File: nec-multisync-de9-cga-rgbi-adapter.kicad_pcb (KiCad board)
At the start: 2 copper layers, 52.1 x 36.1 mm, 8 parts, among them J1 DE9_Plug, J2 DE15_Receptacle_HighDensity, J3 DIN-8

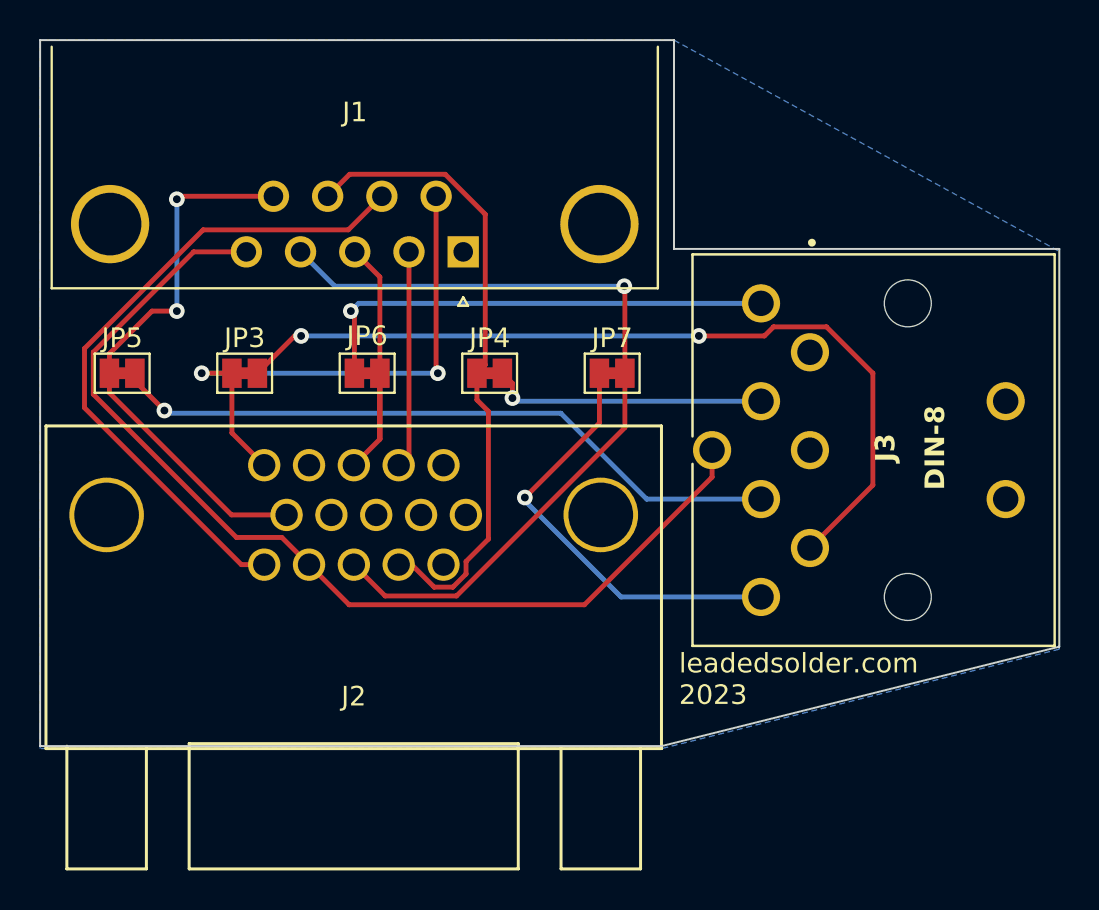
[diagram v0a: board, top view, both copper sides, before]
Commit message: Tie shields together
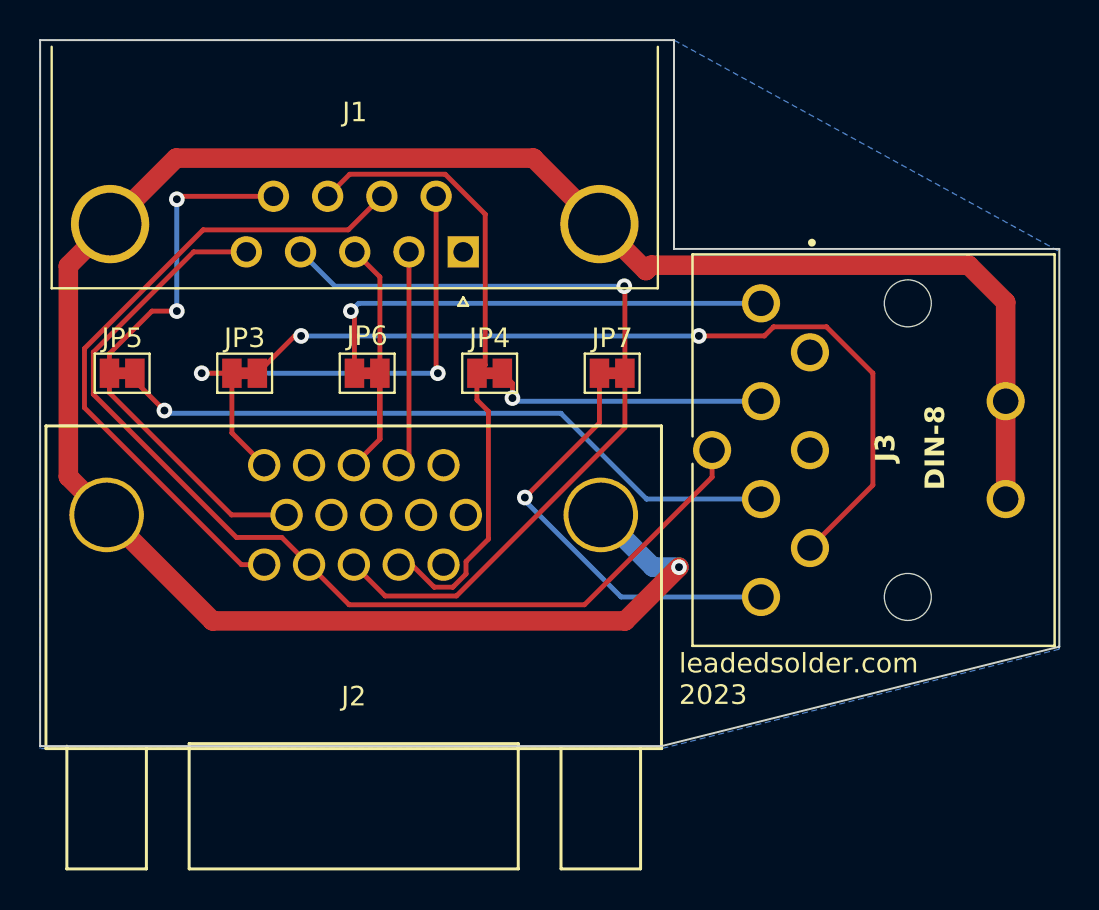
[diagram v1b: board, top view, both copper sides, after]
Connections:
- J1 pad 0: GND -> /Shield
- J2 pad 16: GND -> /Shield
- J2 pad 17: GND -> /Shield
- J3 pad S1: GND -> /Shield
- J3 pad S2: GND -> /Shield
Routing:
- net /Shield: track 0.00 -> 114.8 mm, vias 0 -> 1
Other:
- board text added: "rgbi to nec multisync adapter v0.3"
- board text removed: "rgbi to nec multisync adapter v0.2"
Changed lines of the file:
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@@
   (net 20 "/P6_Red")
   (net 21 "/P6_Green")
+  (net 22 "/Shield")
   (footprint "Jumper:SolderJumper-2_P1.3mm_Bridged_Pad1.0x1.5mm" (layer "F.Cu")
     (at 119.126 90.17)
@@
       (net 7 "/EGA_Blue1") (pintype "passive"))
     (pad "16" thru_hole circle (at 12.6238 11.811 180) (size 3.81 3.81) (drill 3.302) (layers "*.Cu" "*.Mask")
-      (net 1 "GND"))
+      (net 22 "/Shield") (pinfunction "Shield") (pintype "power_in"))
     (pad "17" thru_hole circle (at -12.6238 11.811 180) (size 3.81 3.81) (drill 3.302) (layers "*.Cu" "*.Mask")
-      (net 1 "GND"))
+      (net 22 "/Shield") (pinfunction "Shield") (pintype "power_in"))
     (model "${KICAD7_3DMODEL_DIR}/Connector_Dsub.3dshapes/DSUB-15-HD_Female_Horizontal_P2.29x1.98mm_EdgePinOffset9.40mm.step"
       (offset (xyz -4.5 -13.5 0))
@@
       (net 5 "/EGA_Blue0") (pintype "passive"))
     (pad "S1" thru_hole circle (at -2.5 10 90) (size 1.95 1.95) (drill 1.3) (layers "*.Cu" "*.Mask")
-      (net 1 "GND"))
+      (net 22 "/Shield") (pinfunction "Shield") (pintype "power_in"))
     (pad "S2" thru_hole circle (at 2.5 10 90) (size 1.95 1.95) (drill 1.3) (layers "*.Cu" "*.Mask")
-      (net 1 "GND"))
+      (net 22 "/Shield") (pinfunction "Shield") (pintype "power_in"))
   )
   (footprint "Connector_Dsub:DSUB-9_Male_Horizontal_P2.77x2.84mm_EdgePinOffset7.70mm_Housed_MountingHolesOffset9.12mm" (layer "F.Cu")
@@
       (stroke (width 0.1) (type solid)) (layer "F.Fab"))
     (pad "0" thru_hole circle (at -6.96 1.42 180) (size 4 4) (drill 3.2) (layers "*.Cu" "*.Mask")
-      (net 1 "GND"))
+      (net 22 "/Shield") (pinfunction "Shield") (pintype "power_in"))
     (pad "0" thru_hole circle (at 18.04 1.42 180) (size 4 4) (drill 3.2) (layers "*.Cu" "*.Mask")
-      (net 1 "GND"))
+      (net 22 "/Shield") (pinfunction "Shield") (pintype "power_in"))
     (pad "1" thru_hole rect (at 0 0 180) (size 1.6 1.6) (drill 1) (layers "*.Cu" "*.Mask")
       (net 1 "GND") (pinfunction "1") (pintype "passive"))
@@
     (effects (font (size 1 1) (thickness 0.15)) (justify left bottom mirror))
   )
-  (gr_text "rgbi to nec multisync adapter v0.2" (at 131.000001 89.408 180) (layer "B.SilkS" knockout)
+  (gr_text "rgbi to nec multisync adapter v0.3" (at 131.000001 89.408 180) (layer "B.SilkS" knockout)
     (effects (font (size 1 1) (thickness 0.15)) (justify mirror))
   )
@@
   (segment (start 139.7 96.683097) (end 139.7 96.52) (width 0.25) (layer "B.Cu") (net 21))
   (segment (start 144.616903 101.6) (end 139.7 96.683097) (width 0.25) (layer "B.Cu") (net 21))
+  (segment (start 144.8255 102.8245) (end 147.574 100.076) (width 1) (layer "F.Cu") (net 22))
+  (segment (start 146.16 84.65) (end 145.885 84.925) (width 1) (layer "F.Cu") (net 22))
+  (segment (start 143.51 82.55) (end 140.14 79.18) (width 1) (layer "F.Cu") (net 22))
+  (segment (start 164.265 86.541) (end 162.374 84.65) (width 1) (layer "F.Cu") (net 22))
+  (segment (start 145.885 84.925) (end 143.51 82.55) (width 1) (layer "F.Cu") (net 22))
+  (segment (start 164.265 96.6) (end 164.265 91.6) (width 1) (layer "F.Cu") (net 22))
+  (segment (start 118.332 97.409) (end 123.7475 102.8245) (width 1) (layer "F.Cu") (net 22))
+  (segment (start 116.376 84.684) (end 116.376 95.453) (width 1) (layer "F.Cu") (net 22))
+  (segment (start 121.88 79.18) (end 118.51 82.55) (width 1) (layer "F.Cu") (net 22))
+  (segment (start 118.51 82.55) (end 116.376 84.684) (width 1) (layer "F.Cu") (net 22))
+  (segment (start 164.265 91.6) (end 164.265 86.541) (width 1) (layer "F.Cu") (net 22))
+  (segment (start 162.374 84.65) (end 146.16 84.65) (width 1) (layer "F.Cu") (net 22))
+  (segment (start 140.14 79.18) (end 121.88 79.18) (width 1) (layer "F.Cu") (net 22))
+  (segment (start 116.376 95.453) (end 118.332 97.409) (width 1) (layer "F.Cu") (net 22))
+  (segment (start 123.7475 102.8245) (end 144.8255 102.8245) (width 1) (layer "F.Cu") (net 22))
+  (via (at 147.574 100.076) (size 0.8) (drill 0.4) (layers "F.Cu" "B.Cu") (net 22))
+  (segment (start 146.2466 100.076) (end 143.5796 97.409) (width 1) (layer "B.Cu") (net 22))
+  (segment (start 147.574 100.076) (end 146.2466 100.076) (width 1) (layer "B.Cu") (net 22))
   (zone (net 1) (net_name "GND") (layer "B.Cu") (hatch edge 0.5)
     (connect_pads (clearance 0.5))
